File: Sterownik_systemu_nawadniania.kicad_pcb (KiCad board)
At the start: 2 copper layers, 77.7 x 134.2 mm, 87 parts, among them IC1 STM32F030C6T6, J1 CON-SOCJ-2155, J2 Conn_01x05_Male, J3 Conn_01x16_Female, J4 Screw_Terminal_01x02, J5 Screw_Terminal_01x02, J6 Screw_Terminal_01x02, J7 Screw_Terminal_01x02, J8 Screw_Terminal_01x02, K1 1461103-1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

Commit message: PCB update
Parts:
- K1, K2, K3, K4: value 1461103-1 -> 6-1419128-4
- moved C6 19.9 mm to (154.6, 131.1), turned to -90 degrees
- moved IC1 18.7 mm to (143.9, 119.5)
- moved C3 17.8 mm to (139.5, 126.8), turned to -90 degrees
- moved C1 17.2 mm to (141.1, 126.8), turned to -90 degrees
- moved Y1 16.9 mm to (152.2, 129.5), turned to 90 degrees
- moved C7 15.0 mm to (154.6, 127.9)
- moved R6 12.7 mm to (143.2, 126.8)
- moved C2 12.6 mm to (145.5, 126.8), turned to -90 degrees
- moved L1 12.6 mm to (154.6, 149.8), turned to 180 degrees
- moved C9 12.4 mm to (147.5, 126.8)
- moved C8 12.0 mm to (149.1, 126.8)
- moved C21 11.4 mm to (151.8, 138.3)
- moved C20 11.2 mm to (158.3, 138.3)
- moved C19 8.40 mm to (160.3, 152.0), turned to 0 degrees
- moved C17 5.49 mm to (163.7, 137.4), turned to -90 degrees
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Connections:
- D1 pad C: VDD -> +24V
- D2 pad C: VDD -> +24V
- D3 pad C: VDD -> +24V
- D4 pad C: VDD -> +24V
- K1 pad 2: VDD -> +24V
- K2 pad 2: VDD -> +24V
- K3 pad 2: VDD -> +24V
- K4 pad 2: VDD -> +24V
- U3 pad 10: VDD -> +24V
- U3 pad 12: VDD -> +24V
- U3 pad 14: VDD -> +24V
- U3 pad 16: VDD -> +24V
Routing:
- net VDD: track 422.8 -> 172.7 mm, vias 6 -> 2
- net +24V: track 132.4 -> 0.00 mm
- net /Valve_1: track 64.8 -> 0.00 mm, vias 2 -> 0
- net /Valve_3: track 56.5 -> 0.00 mm, vias 2 -> 0
- net /NRST: track 73.4 -> 17.4 mm, vias 2 -> 0
- net /Valve_2: track 52.6 -> 0.00 mm, vias 2 -> 0
- net /Btn_1: track 64.1 -> 11.6 mm, vias 2 -> 0
- net /Valve_4: track 43.3 -> 0.00 mm, vias 2 -> 0
- net Net-(R28-Pad1): track 40.3 -> 0.00 mm, vias 2 -> 0
- net /Btn_2: track 78.0 -> 38.6 mm, vias 2 -> 0
- net /Rain_sensor: track 38.8 -> 0.00 mm, vias 2 -> 0
- net /ESP_NRST: track 34.2 -> 0.00 mm
- net /Btn_3: track 37.3 -> 5.83 mm, vias 2 -> 1
- net Net-(R27-Pad1): track 28.6 -> 0.00 mm
- net /Btn_4: track 32.5 -> 6.43 mm, vias 2 -> 0
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
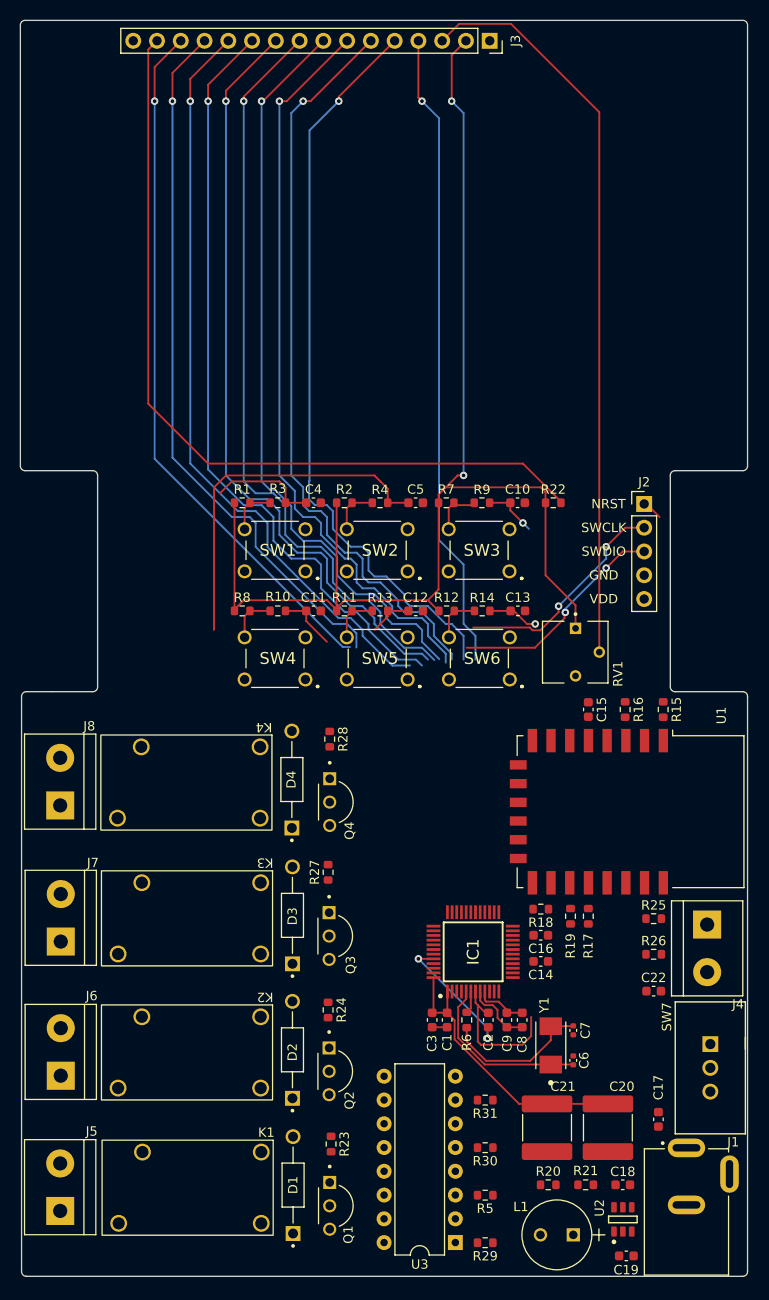
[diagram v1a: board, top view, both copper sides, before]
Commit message: Routing and keep out zones
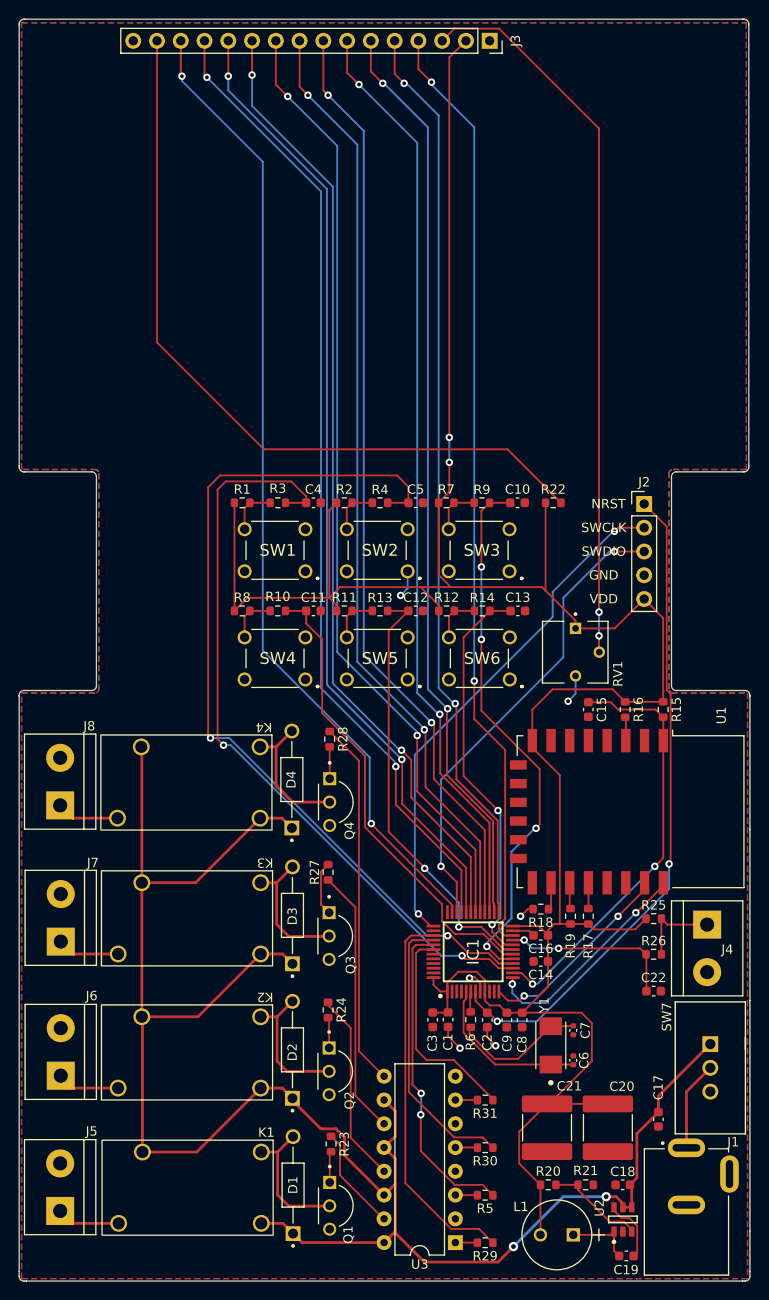
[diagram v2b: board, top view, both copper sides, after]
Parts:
- moved R6 0.42 mm to (143.6, 126.7)
- moved C1 0.11 mm to (141.2, 126.7)
- moved C2 0.10 mm to (145.4, 126.8)
- moved C3 0.06 mm to (139.6, 126.8)
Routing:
- net +24V: track 0.00 -> 201.2 mm, vias 0 -> 2
- net VDD: track 172.7 -> 282.4 mm
- net /Btn_1: track 11.6 -> 81.8 mm, vias 0 -> 2
- net /Btn_2: track 38.6 -> 95.6 mm, vias 0 -> 2
- net /NRST: track 17.4 -> 70.8 mm, vias 0 -> 2
- net /Btn_3: track 5.83 -> 58.3 mm, vias 1 -> 4
- net /ESP_NRST: track 0.00 -> 45.9 mm, vias 0 -> 2
- net /Btn_4: track 6.43 -> 50.4 mm
- net /Btn_5: track 4.83 -> 46.7 mm, vias 0 -> 2
- net /Valve_1: track 0.00 -> 41.1 mm
- net Net-(R28-Pad1): track 0.00 -> 39.3 mm
- net /Btn_6: track 5.47 -> 42.5 mm, vias 1 -> 2
- net /Valve_3: track 0.00 -> 34.1 mm, vias 0 -> 2
- net /DISP_RS: track 68.7 -> 100.9 mm, vias 1 -> 2
- net /SWCLK: track 24.1 -> 55.5 mm
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- added copper zone on B.Cu, net GND
- added copper zone on F.Cu, net GND
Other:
- board size 77.7 x 134.2 mm -> 78.1 x 134.9 mm

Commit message: lab 14:40
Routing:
- net /DISP_DB1: track 100.3 -> 100.9 mm, vias 2 -> 1
- net /DISP_RW: track 98.0 -> 98.3 mm, vias 2 -> 1
- net /DISP_DB4: track 102.9 -> 103.1 mm, vias 2 -> 1
- net /DISP_DB0: track 99.5 -> 99.4 mm, vias 2 -> 1
- net /DISP_E: track 98.8 -> 98.7 mm, vias 2 -> 1
- net /DISP_RS: vias 2 -> 1
- net /DISP_DB3: vias 2 -> 1
- net /DISP_DB2: vias 2 -> 1
- net /DISP_DB7: vias 2 -> 1
- net /DISP_DB6: vias 2 -> 1
- net /DISP_DB5: vias 2 -> 1
